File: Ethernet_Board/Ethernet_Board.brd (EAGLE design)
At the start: 57 x 41 mm, 36 parts, among them J1 22-05-7028-02, J2 22-05-7068-06, J3 22-05-7068-06, P1 RB1-125BAG1A, T1 EXMACHINA-LOGO-NAME, U1 DP83848JSQ/NOPB, X1 ASE_50

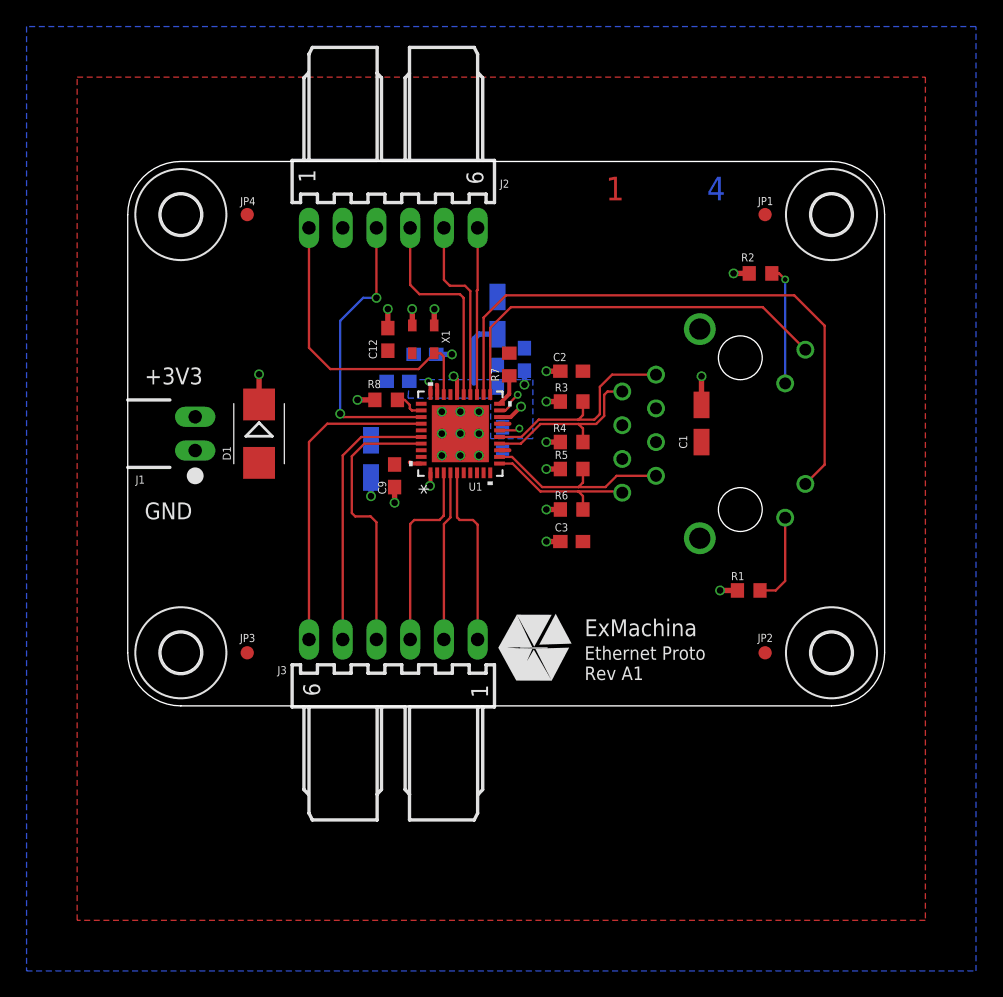
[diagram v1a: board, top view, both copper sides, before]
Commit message: Replace output connector and generate gerber files
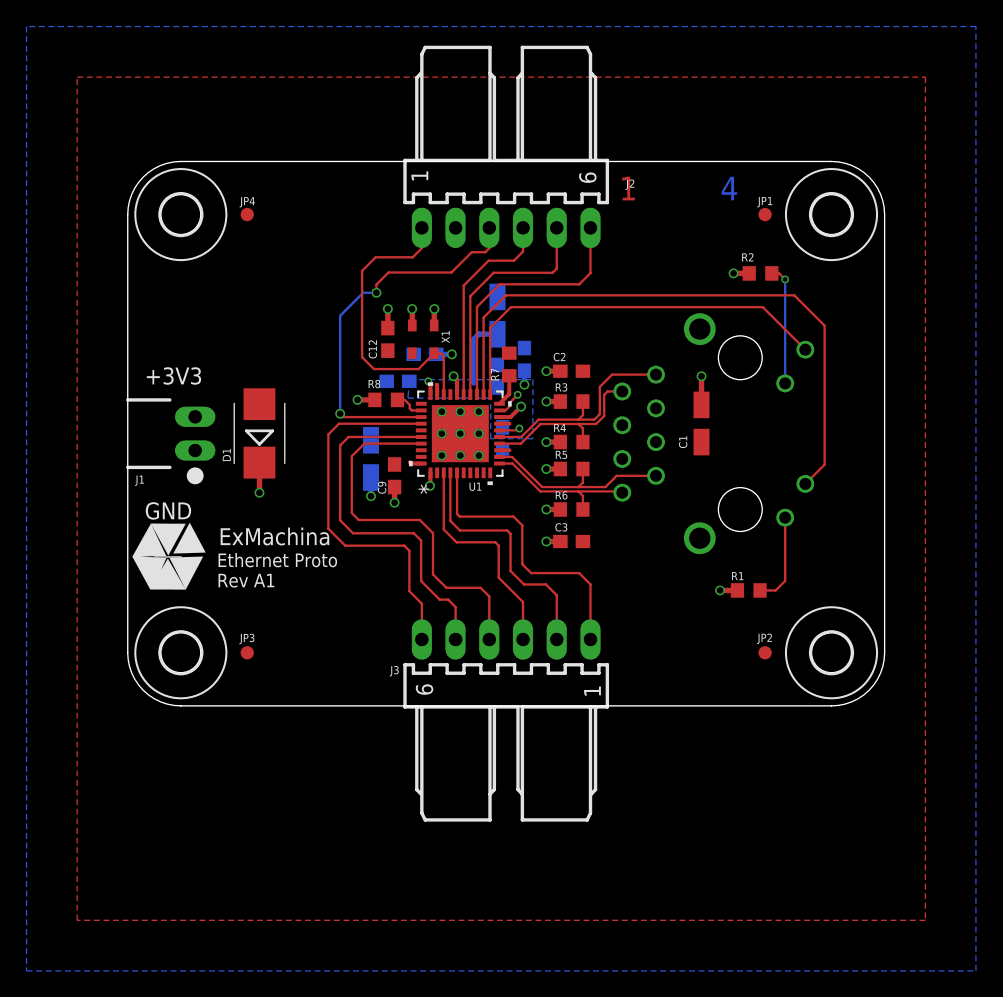
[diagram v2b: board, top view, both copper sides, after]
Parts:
- moved T1 28.4 mm to (3.03, 11.2)
- moved J2 8.50 mm to (28.5, 36.0)
- moved J3 8.50 mm to (28.5, 5.00)
- turned D1 to 90 degrees
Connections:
- net +3V3: now also J1.1; no longer J1.2
- net GND: now also J1.2; no longer J1.1
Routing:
- net ETH_TXD_1: track 13.8 -> 21.2 mm
- net ETH_RXD_0: track 20.3 -> 27.6 mm
- net ETH_RXD_1: track 20.9 -> 27.9 mm
- net ETH_RST: track 12.6 -> 19.6 mm
- net ETH_CRS: track 21.9 -> 28.8 mm
- net ETH_TXD_0: track 12.8 -> 18.9 mm
- net ETH_RX_ER: track 23.9 -> 28.3 mm
- net ETH_MDIO: track 14.0 -> 17.9 mm
- net ETH_TXD_EN: track 14.7 -> 16.7 mm
